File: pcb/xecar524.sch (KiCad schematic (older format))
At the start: 33 parts, among them J1 JTAG, J3 CFG, U1 MCP1703A-3302_SOT89, U2 Atari_XE_Cartridge_Connector, U3 XC95144XL-TQ100, U4 SST39VF040

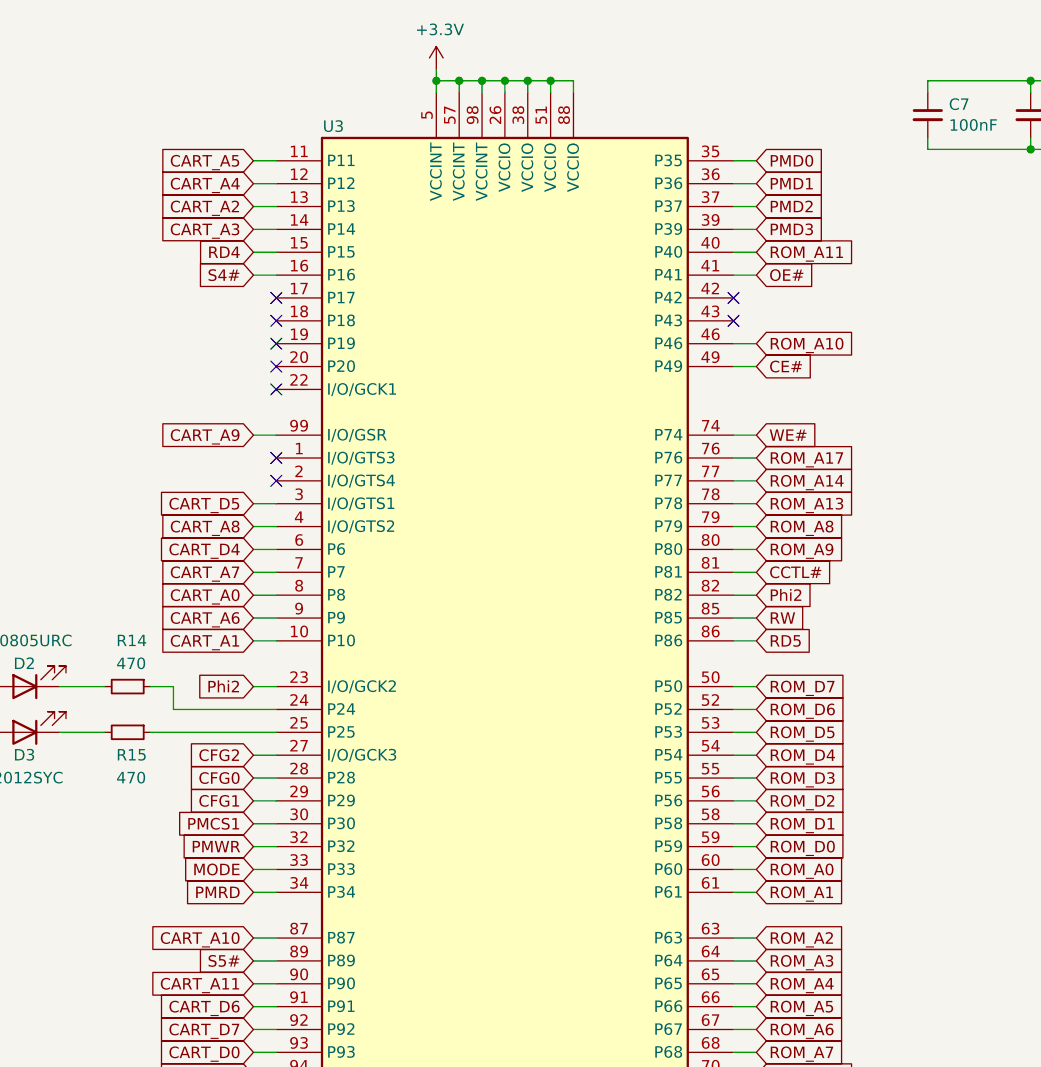
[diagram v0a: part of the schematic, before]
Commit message: Switch to PIC24FJ64GB004 as RTime8 emulator
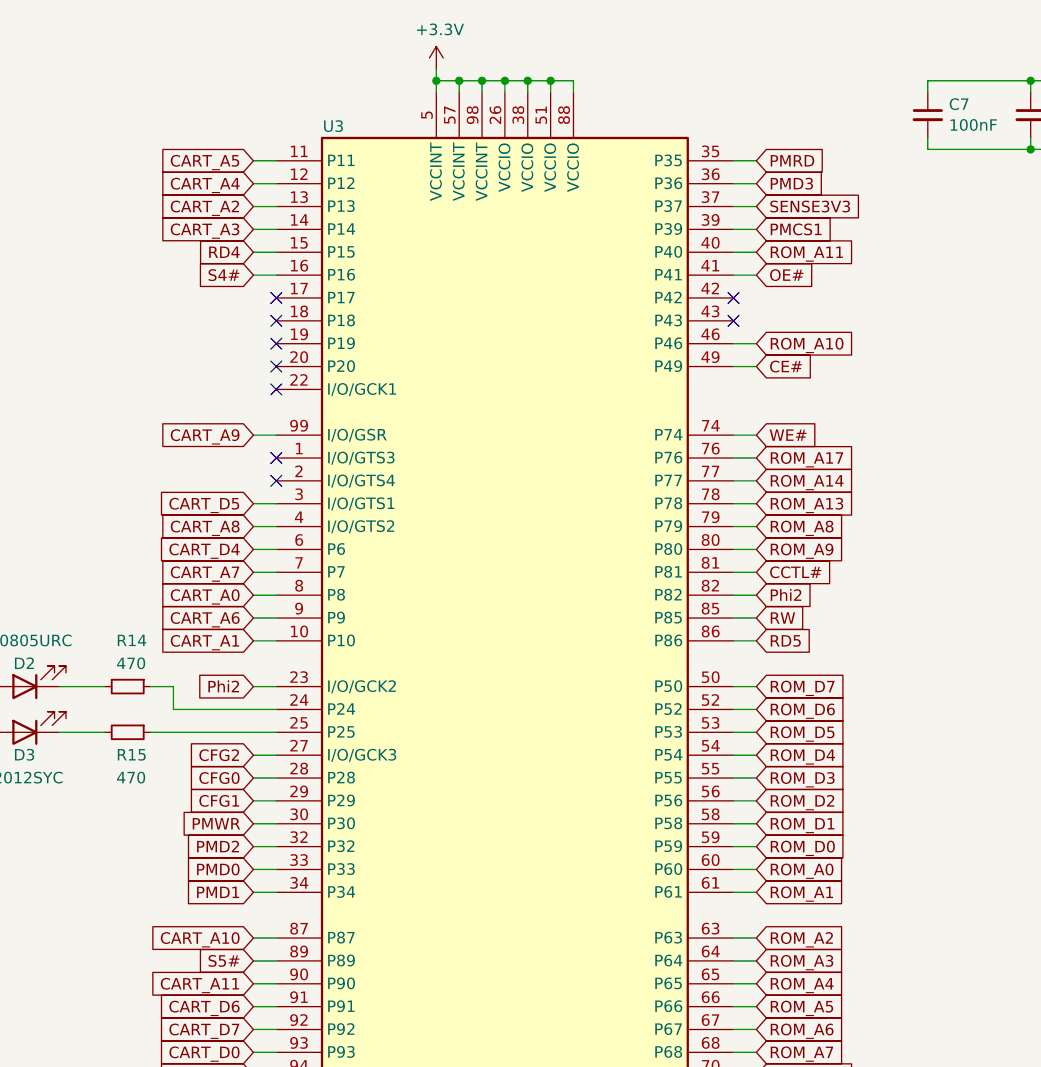
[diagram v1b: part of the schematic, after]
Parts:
- LOGO1: footprint Symbol:OSHW-Symbol_13.4x12mm_Copper -> Symbol:OSHW-Symbol_8.9x8mm_Copper
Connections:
- net MODE is gone; now on net PMD0: U3.33 (P33)
- net PMCS1: now also U3.39 (P39); no longer U3.30 (P30)
- net PMD0: no longer U3.35 (P35)
- net PMD1: now also U3.34 (P34); no longer U3.36 (P36)
- net PMD2: now also U3.32 (P32); no longer U3.37 (P37)
- net PMD3: now also U3.36 (P36); no longer U3.39 (P39)
- net PMRD: now also U3.35 (P35); no longer U3.34 (P34)
- net PMWR: now also U3.30 (P30); no longer U3.32 (P32)
- new net SENSE3V3: U3.37 (P37)
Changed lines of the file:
@@
 Text GLabel 6900 4050 2    50   Input ~ 0
 ROM_D2
-Text GLabel 4700 4150 0    50   Input ~ 0
+Text GLabel 6900 1550 2    50   Input ~ 0
 PMCS1
+Text GLabel 6900 1250 2    50   Input ~ 0
+PMRD
+Text GLabel 4700 4250 0    50   Input ~ 0
+PMD2
 Text GLabel 4700 4450 0    50   Input ~ 0
-PMRD
-Text GLabel 6900 1450 2    50   Input ~ 0
-PMD2
-Text GLabel 6900 1350 2    50   Input ~ 0
 PMD1
 Wire Wire Line
@@
 Wire Wire Line
 	6900 1650 6800 1650
-Text GLabel 6900 1550 2    50   Input ~ 0
+Text GLabel 6900 1350 2    50   Input ~ 0
 PMD3
-Text GLabel 6900 1250 2    50   Input ~ 0
+Text GLabel 4700 4350 0    50   Input ~ 0
 PMD0
 Wire Wire Line
@@
 	1    0    0    -1
 $EndComp
-Text GLabel 4700 4250 0    50   Input ~ 0
+Text GLabel 4700 4150 0    50   Input ~ 0
 PMWR
 Wire Wire Line
@@
 F 0 "LOGO1" H 1150 7325 50  0001 C CNN
 F 1 "Logo_Open_Hardware_Small" H 1150 6825 50  0001 C CNN
-F 2 "Symbol:OSHW-Symbol_13.4x12mm_Copper" H 1150 7050 50  0001 C CNN
+F 2 "Symbol:OSHW-Symbol_8.9x8mm_Copper" H 1150 7050 50  0001 C CNN
 F 3 "~" H 1150 7050 50  0001 C CNN
 	1    1150 7050
@@
 Text GLabel 4700 3850 0    50   Input ~ 0
 CFG2
-Text GLabel 4700 4350 0    50   Input ~ 0
-MODE
 Wire Wire Line
 	4700 4150 4800 4150
+Text GLabel 6900 1450 2    50   Input ~ 0
+SENSE3V3
 $EndSCHEMATC
